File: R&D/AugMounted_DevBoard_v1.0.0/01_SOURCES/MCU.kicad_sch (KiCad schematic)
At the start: 5 parts, among them J1 J_TYPE-C-31-M-13, U1 ESP32-S3-WROOM-1U-N16R8

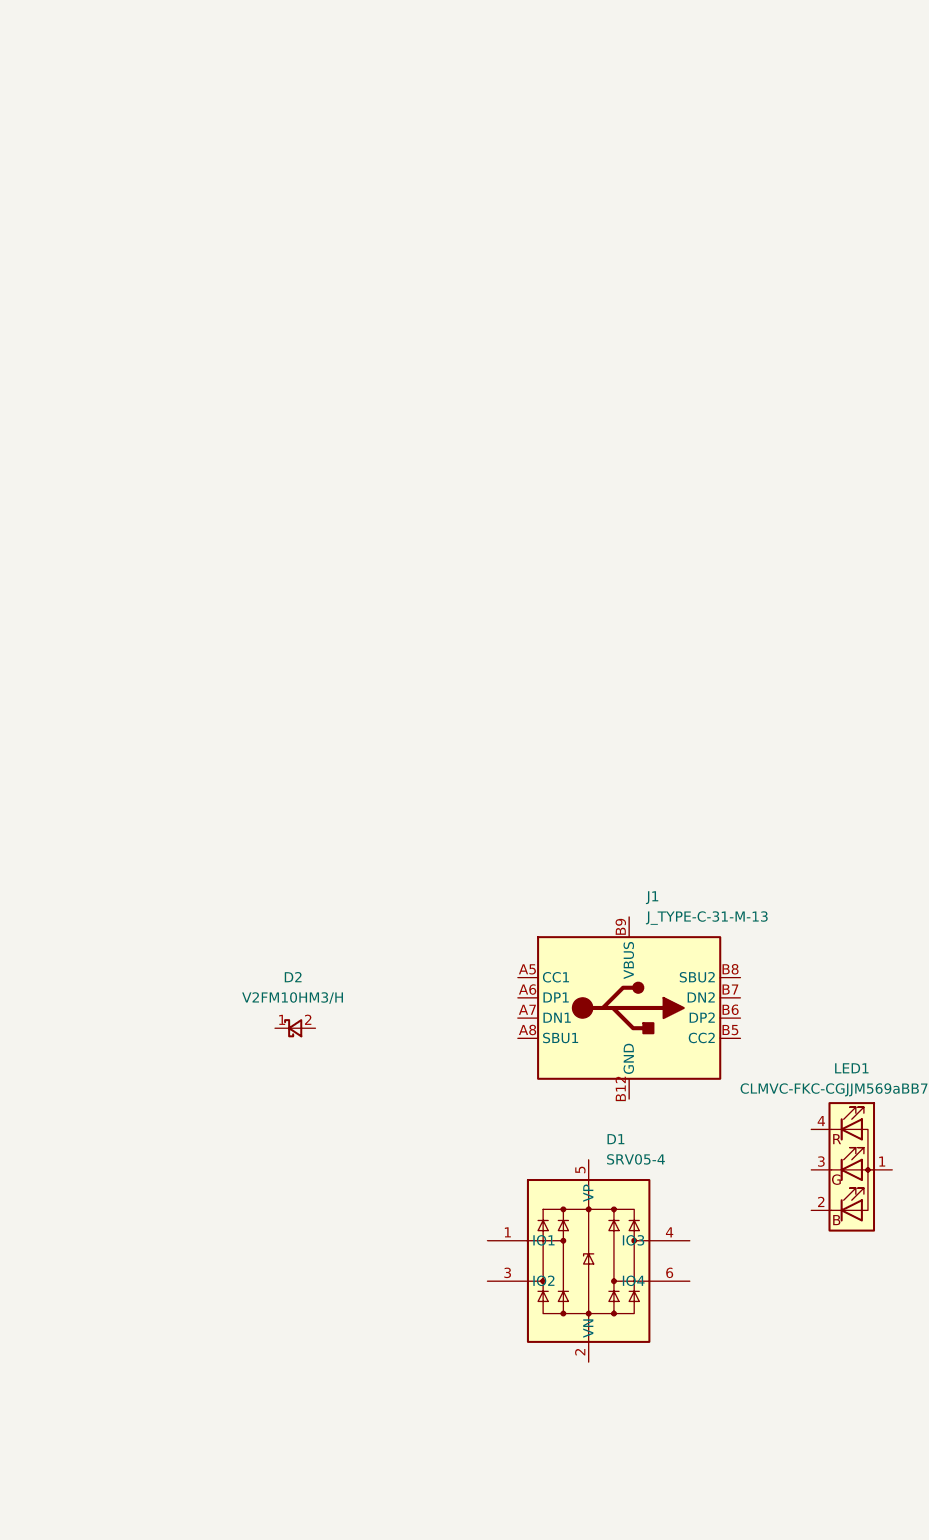
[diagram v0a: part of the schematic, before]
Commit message: Major components are done in library
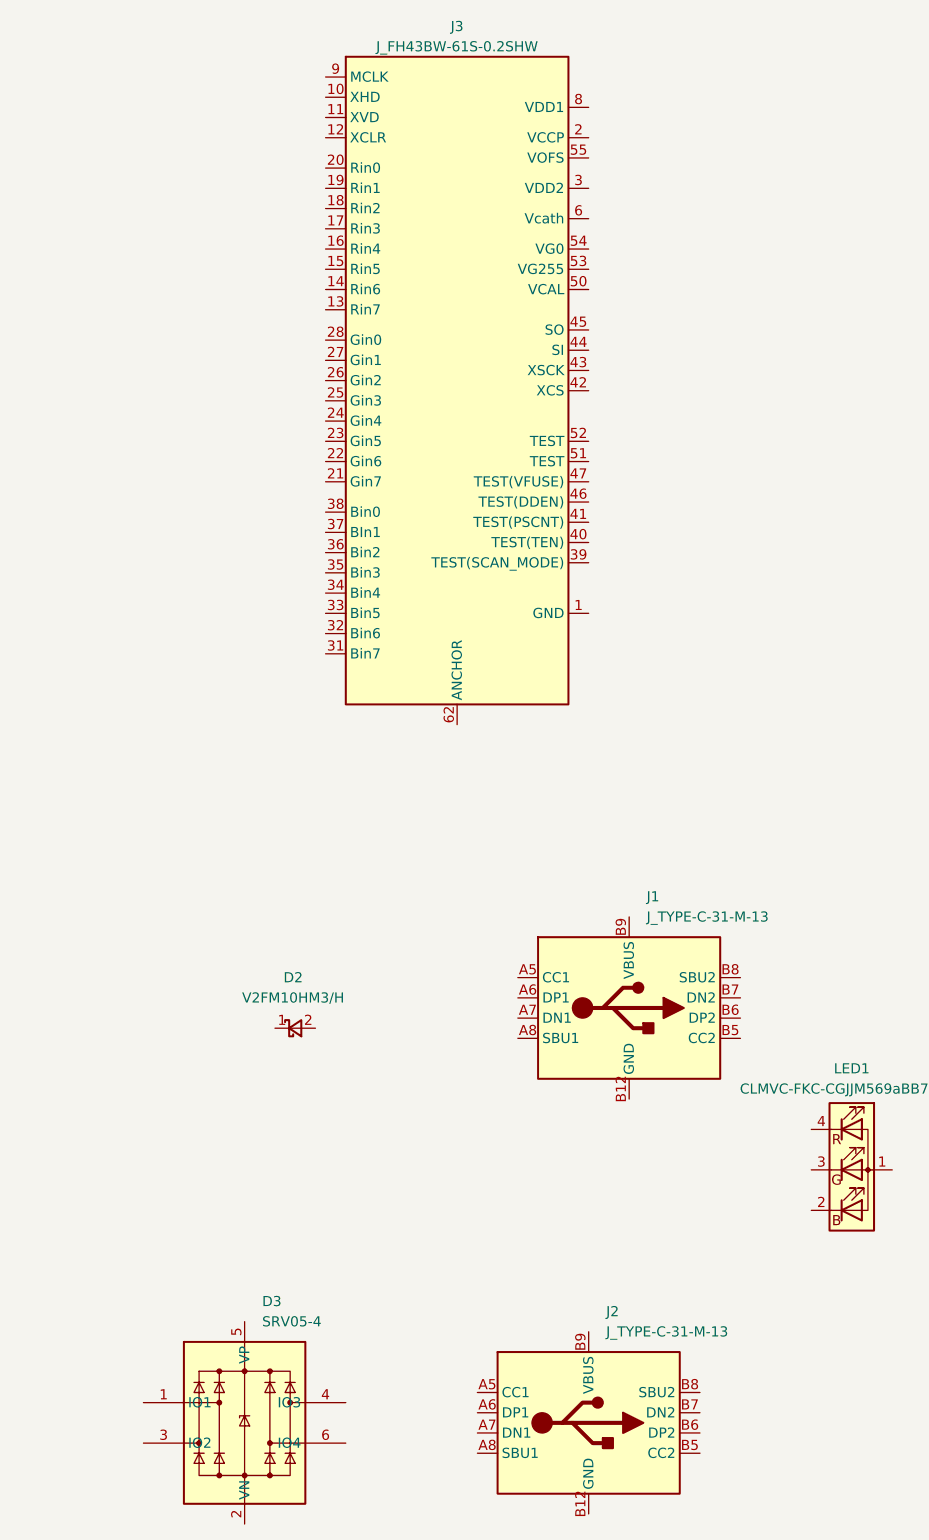
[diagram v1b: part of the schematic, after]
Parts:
- removed D1: D_SRV05-4, .mounted-lib:SOT-23-6_TECH_PUBLIC, symbol .mounted-lib:D_SRV05-4
- added D3: D_SRV05-4, .mounted-lib:SOT-23-6_TECH_PUBLIC, symbol .mounted-lib:D_SRV05-4
- added J2: J_TYPE-C-31-M-13, .mounted-lib:J_TYPE-C-31-M-13, symbol .mounted-lib:J_TYPE-C-31-M-13
- added J3: J_FH43BW-61S-0.2SHW, .mounted-lib:J_FH43BW-61S-0.2SHW, symbol .mounted-lib:J_ECX333A
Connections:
- new net: J2.A1 (GND), J2.A12 (GND), J2.B1 (GND), J2.B12 (GND), J2.GND
- new net: J2.A4 (VBUS), J2.A9 (VBUS), J2.B4 (VBUS), J2.B9 (VBUS)
- new net: J3.1 (GND), J3.30 (GND), J3.4 (GND), J3.48 (GND), J3.5 (GND), J3.57 (GND), J3.58 (GND), J3.61 (GND), J3.7 (GND)
- new net: J3.2 (VCCP), J3.60 (VCCP)
- new net: J3.29 (VDD1), J3.49 (VDD1), J3.8 (VDD1)
- new net: J3.3 (VDD2), J3.59 (VDD2)
- new net: J3.56 (Vcath), J3.6 (Vcath)
- new net: J3.62 (ANCHOR), J3.63 (ANCHOR)

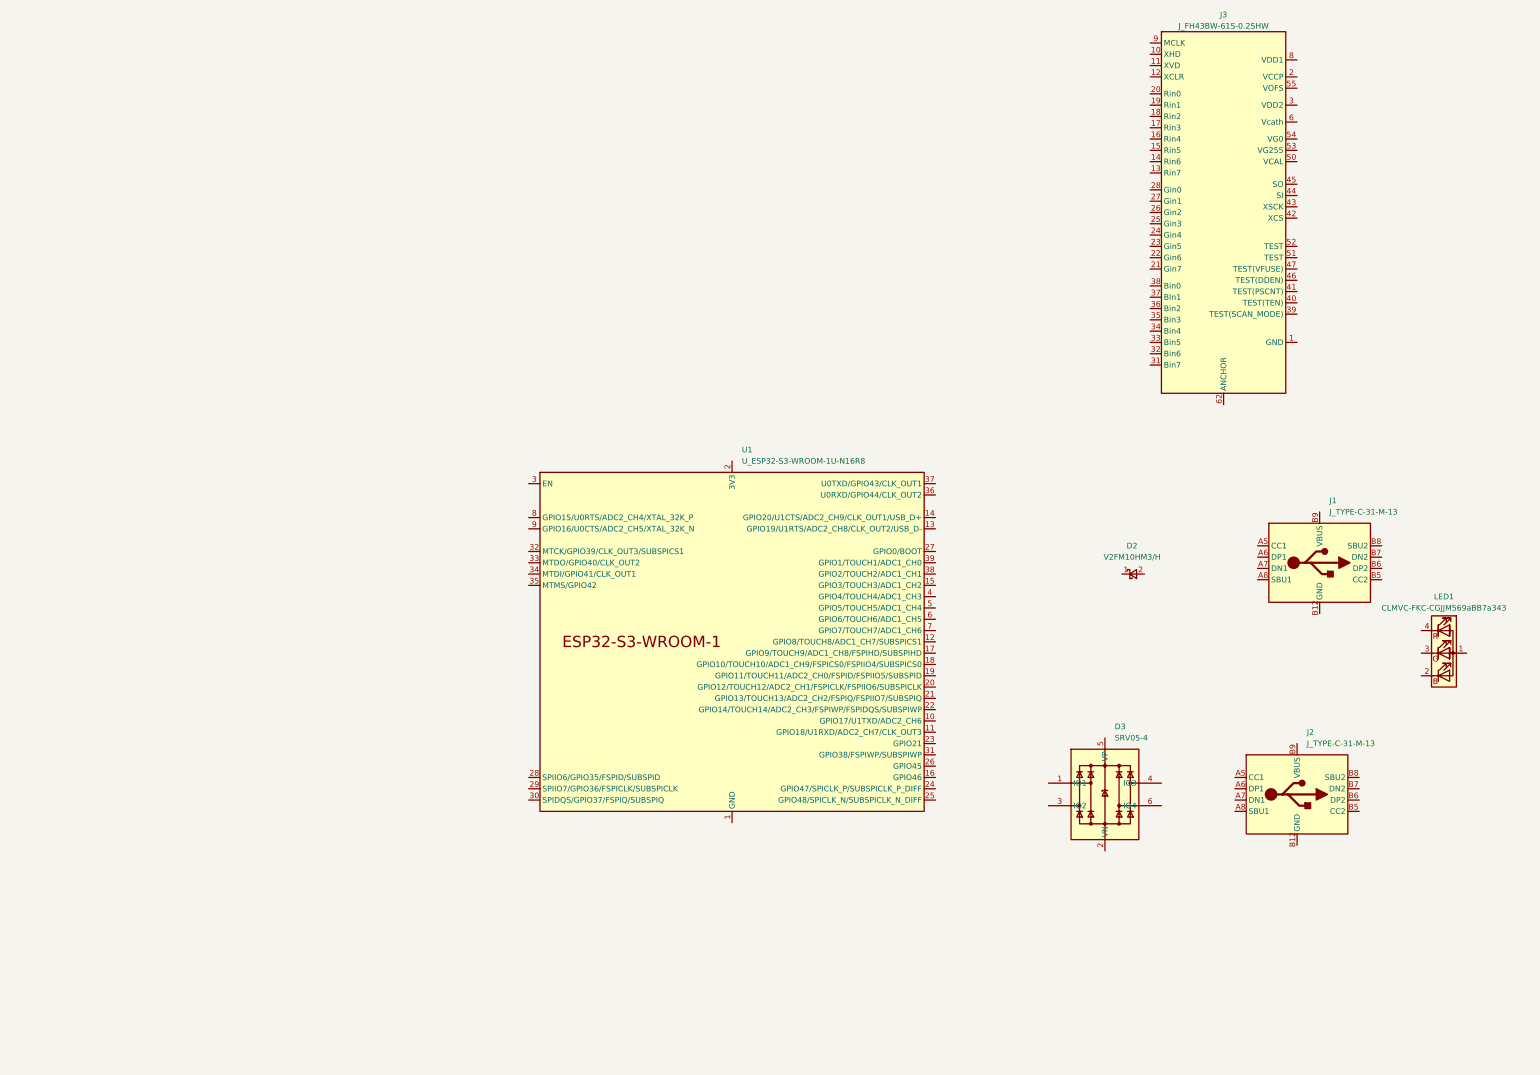
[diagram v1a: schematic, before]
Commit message: Created all components, placed them, and added images of typical applications. ECX334A and ESP32-S3 pdf are available in 00_RESOURCES
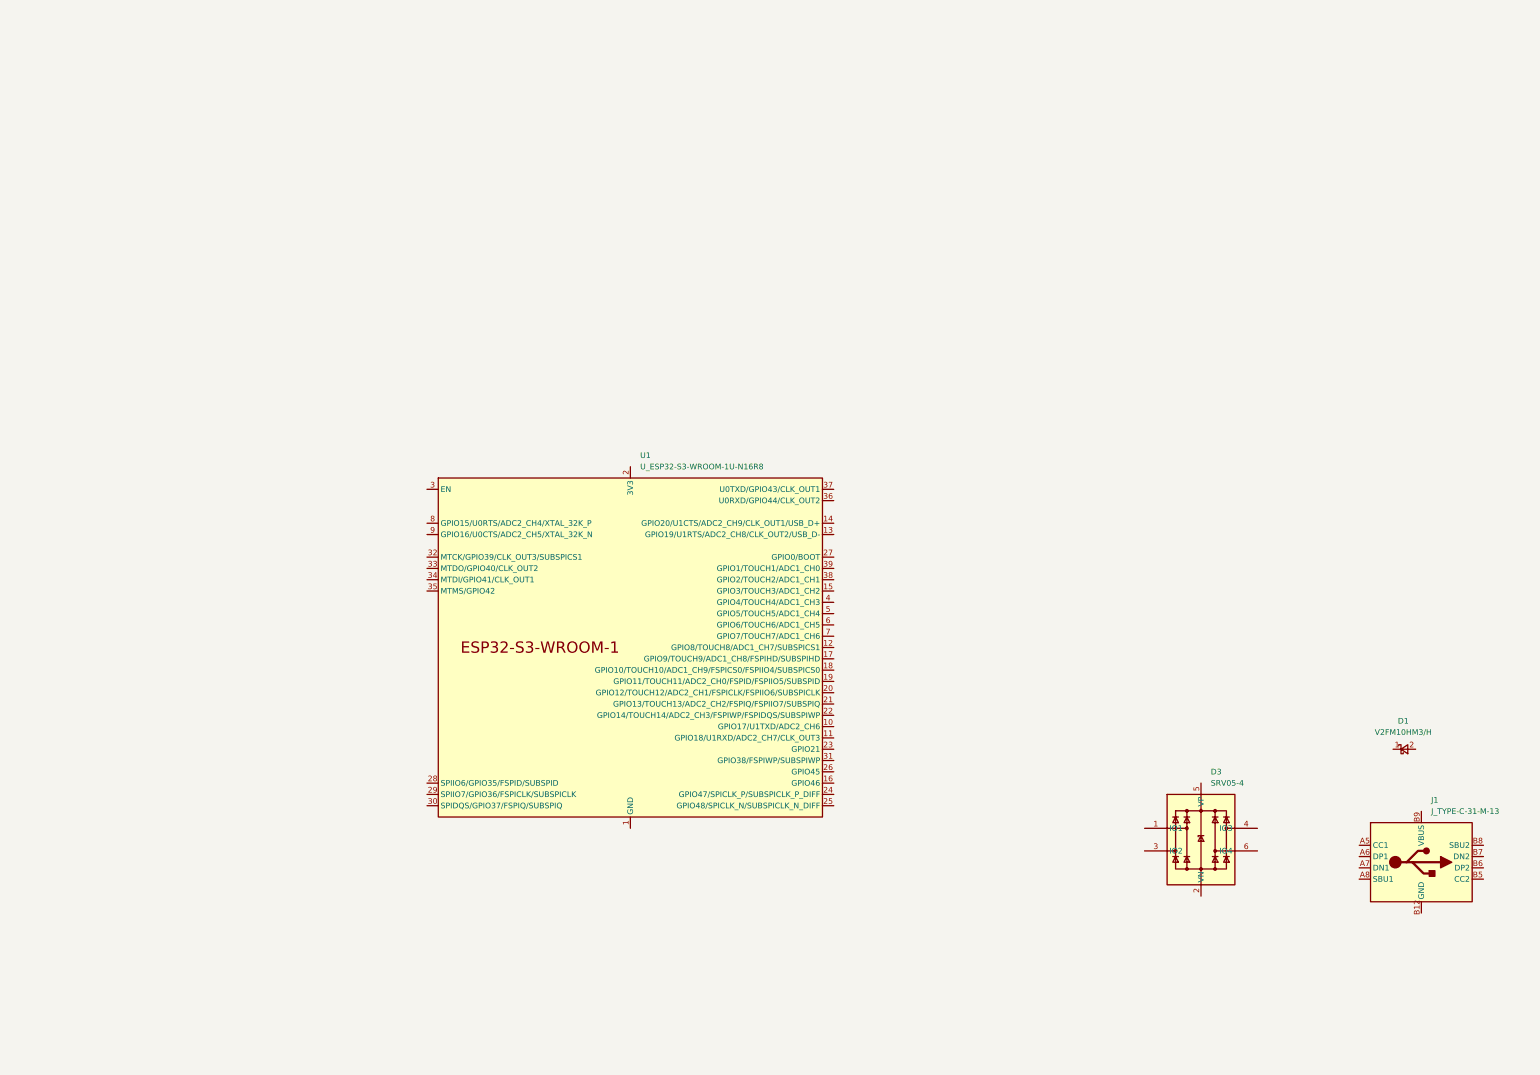
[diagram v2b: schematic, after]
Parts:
- removed D2: D_V2FM10HM3/H, .gouach-lib:D_SMF_VISHAY, symbol .mounted-lib:D_V2FM10HM3/H
- removed J2: J_TYPE-C-31-M-13, .mounted-lib:J_TYPE-C-31-M-13, symbol .mounted-lib:J_TYPE-C-31-M-13
- removed J3: J_FH43BW-61S-0.2SHW, .mounted-lib:J_FH43BW-61S-0.2SHW, symbol .mounted-lib:J_ECX333A
- removed LED1: LED_CLMVC_FKC_CGJJM569aBB7a343, .gouach-lib:LED_CLMVC-FKC-CGJJM569aBB7a343, symbol .mounted-lib:LED_CLMVC_FKC_CGJJM569aBB7a343
- added D1: D_V2FM10HM3/H, .mounted-lib:D_SMF_VISHAY, symbol .mounted-lib:D_V2FM10HM3/H
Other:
- moved on the sheet: D3, U1

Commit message: Schematic 90% done
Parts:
- added C29: C_0603_100nF_100V_X7R_10%, .mounted-lib:C_0603_1608Metric, symbol .mounted-lib:C_0603_100nF_100V_X7R_10%
- added C30: C_0603_2.2uF_10V_X7R_10%, .mounted-lib:C_0603_1608Metric, symbol .mounted-lib:C_0603_2.2uF_10V_X7R_10%
- added U9: U_VCNL4040M3OE, .mounted-lib:VCNL4040_4X2X1.1_VISHAY, symbol .mounted-lib:U_VCNL4040M3OE
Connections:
- net VBUS: now reaches D1.1 (K)
- net VBUS_USB: now reaches D1.2 (A)
- net VBUS_USB: now also D3.5 (VP), J1.A4 (VBUS), J1.A9 (VBUS), J1.B4 (VBUS), J1.B9 (VBUS)
- net GND: now reaches J1.A1 (GND), J1.A12 (GND), J1.B1 (GND), J1.B12 (GND), J1.GND
- net GND: now also D3.2 (VN), U1.1 (GND), U1.40 (GND), U1.41 (GND), C29.2, C30.2, U9.1 (GND)
- net USB_D+: now reaches J1.A6 (DP1)
- net USB_D+: now also D3.1 (IO1), J1.B6 (DP2), U1.14 (GPIO20/U1CTS/ADC2_CH9/CLK_OUT1/USB_D+)
- net USB_D-: now reaches J1.A7 (DN1)
- net USB_D-: now also D3.4 (IO3), J1.B7 (DN2), U1.13 (GPIO19/U1RTS/ADC2_CH8/CLK_OUT2/USB_D-)
- net CC1: now reaches D3.3 (IO2)
- net CC2: now reaches D3.6 (IO4)
- net SDA: now reaches U1.10 (GPIO17/U1TXD/ADC2_CH6)
- net SDA: now also U9.7 (SDA)
- net SCL: now reaches U1.11 (GPIO18/U1RXD/ADC2_CH7/CLK_OUT3)
- net SCL: now also U9.8 (SCL)
- net XCLR: now reaches U1.12 (GPIO8/TOUCH8/ADC1_CH7/SUBSPICS1)
- net XHD: now reaches U1.15 (GPIO3/TOUCH3/ADC1_CH2)
- net HVD: now reaches U1.16 (GPIO46)
- net MCLK: now reaches U1.17 (GPIO9/TOUCH9/ADC1_CH8/FSPIHD/SUBSPIHD)
- net B5: now reaches U1.18 (GPIO10/TOUCH10/ADC1_CH9/FSPICS0/FSPIIO4/SUBSPICS0)
- net B4: now reaches U1.19 (GPIO11/TOUCH11/ADC2_CH0/FSPID/FSPIIO5/SUBSPID)
- net B3: now reaches U1.20 (GPIO12/TOUCH12/ADC2_CH1/FSPICLK/FSPIIO6/SUBSPICLK)
- net B2: now reaches U1.21 (GPIO13/TOUCH13/ADC2_CH2/FSPIQ/FSPIIO7/SUBSPIQ)
- net B1: now reaches U1.22 (GPIO14/TOUCH14/ADC2_CH3/FSPIWP/FSPIDQS/SUBSPIWP)
- net G6: now reaches U1.23 (GPIO21)
- net G5: now reaches U1.24 (GPIO47/SPICLK_P/SUBSPICLK_P_DIFF)
- net G4: now reaches U1.25 (GPIO48/SPICLK_N/SUBSPICLK_N_DIFF)
- net G3: now reaches U1.26 (GPIO45)
- net G2: now reaches U1.31 (GPIO38/FSPIWP/SUBSPIWP)
- net G1: now reaches U1.32 (MTCK/GPIO39/CLK_OUT3/SUBSPICS1)
- net R5: now reaches U1.33 (MTDO/GPIO40/CLK_OUT2)
- net R4: now reaches U1.34 (MTDI/GPIO41/CLK_OUT1)
- net R3: now reaches U1.35 (MTMS/GPIO42)
- net R2: now reaches U1.38 (GPIO2/TOUCH2/ADC1_CH1)
- net R1: now reaches U1.39 (GPIO1/TOUCH1/ADC1_CH0)
- net MISO: now reaches U1.4 (GPIO4/TOUCH4/ADC1_CH3)
- net MOSI: now reaches U1.5 (GPIO5/TOUCH5/ADC1_CH4)
- net SCK: now reaches U1.6 (GPIO6/TOUCH6/ADC1_CH5)
- net CS: now reaches U1.7 (GPIO7/TOUCH7/ADC1_CH6)
- net ESP_POWER_EN: now reaches U1.8 (GPIO15/U0RTS/ADC2_CH4/XTAL_32K_P)
- new net: U9.2 (CATHODE_SENSOR), U9.5 (CATHODE_LED)
- new net +3.3V: C29.1, C30.1, U9.3 (VDD), U9.4 (ANODE)
- no-connect marks 0 -> 8
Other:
- moved on the sheet: D1, D3, J1

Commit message: Moved components
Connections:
- net ENCODER_S2: now reaches U1.36 (U0RXD/GPIO44/CLK_OUT2)
- net ENCODER_S1: now reaches U1.37 (U0TXD/GPIO43/CLK_OUT1)
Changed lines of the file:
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@@
+    (effects (font (size 1.27 1.27)) (justify left))
+  )
+  (hierarchical_label "ENCODER_S1" (shape input) (at 139.7 35.56 0) (fields_autoplaced)
     (effects (font (size 1.27 1.27)) (justify left))
   )
@@
     (effects (font (size 1.27 1.27)) (justify left))
   )
+  (hierarchical_label "ENCODER_S2" (shape input) (at 139.7 38.1 0) (fields_autoplaced)
+    (effects (font (size 1.27 1.27)) (justify left))
+  )
